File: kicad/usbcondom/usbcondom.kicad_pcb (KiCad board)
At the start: 4 copper layers, 44 x 29 mm, 21 parts, among them J1 Conn_02x10_Odd_Even, J2 Conn_02x10_Odd_Even, J3 USB-ID, J4 USB, U1 USBLC6-2

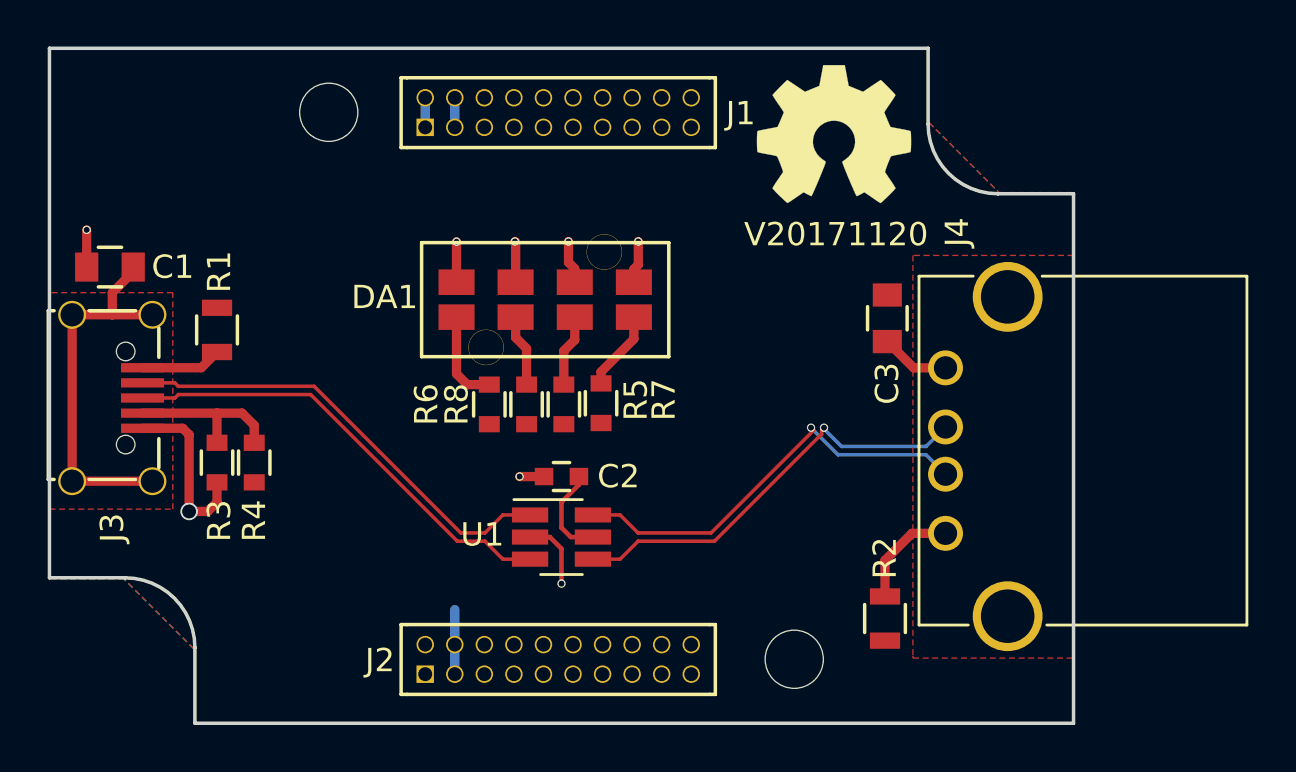
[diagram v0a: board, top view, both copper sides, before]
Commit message: updated silk, added proto area, replaced usb connectors
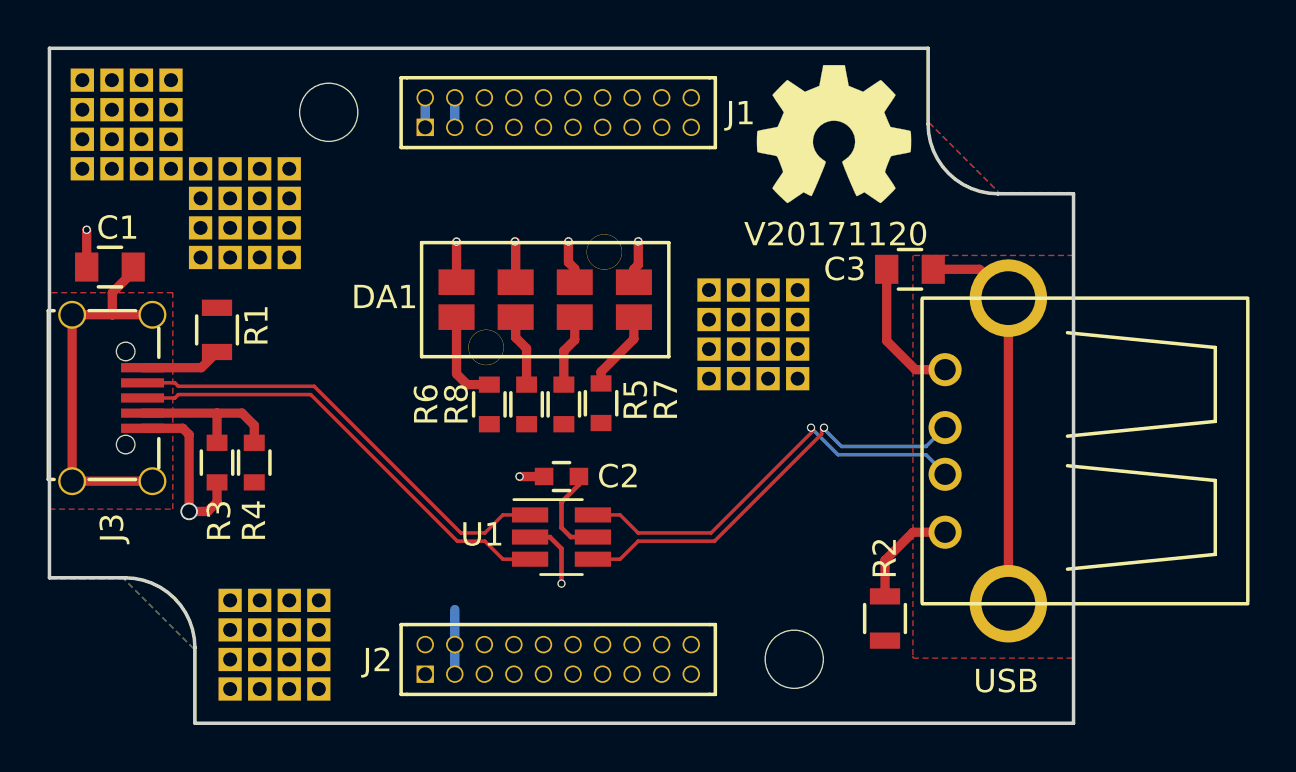
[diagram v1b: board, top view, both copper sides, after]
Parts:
- added J5: Proto, SquantorProto:proto-SMD-0127-04X04-P010-H006, F.Cu at (137.7, 111.1)
- added J6: Proto, SquantorProto:proto-SMD-0127-04X04-P010-H006, F.Cu at (158.2, 97.8)
- added J7: Proto, SquantorProto:proto-SMD-0127-04X04-P010-H006, F.Cu at (136.4, 92.6)
- added J8: Proto, SquantorProto:proto-SMD-0127-04X04-P010-H006, F.Cu at (131.3, 88.8)
- J4: footprint Connectors:USB_A -> SquantorUsb:USB-A-TH
- moved J4 4.45 mm to (169.2, 102.8), turned to 180 degrees
- moved C3 2.32 mm to (165.0, 95.0), turned to 0 degrees
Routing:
- net Net-(C3-Pad2): track 0.00 -> 16.9 mm
- net VSS: track 26.3 -> 29.4 mm

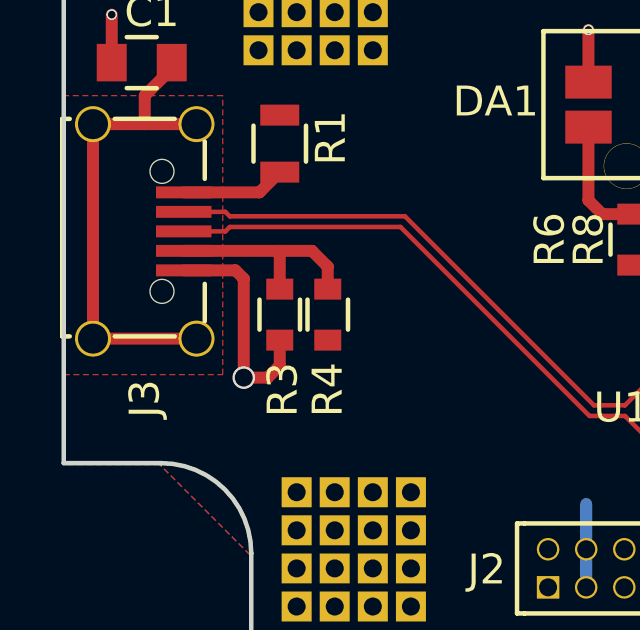
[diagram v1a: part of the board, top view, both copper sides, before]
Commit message: minor layout and silk screen updates
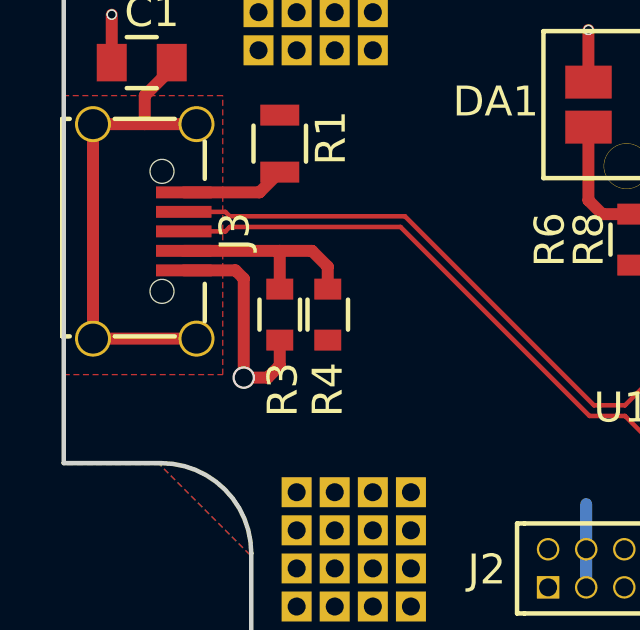
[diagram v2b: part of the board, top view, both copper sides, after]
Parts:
- J3: footprint SquantorUsb:SquantorUsb-USB-UB-SMD4H -> SquantorUsb:USB-muB-SMD_TH
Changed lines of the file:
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@@
   (general
     (links 42)
-    (no_connects 5)
+    (no_connects 0)
     (area 127.924999 85.424999 172.075001 114.575001)
     (thickness 1.6)
@@
       (net 36 /DIGITAL_15))
   )
-  (module SquantorUsb:SquantorUsb-USB-UB-SMD4H (layer F.Cu)
-    (at 130.7 100.525 270)
-    (fp_text reference J3 (at 5.575 0 270) (layer F.SilkS)
-      (effects (font (size 1 1) (thickness 0.15)))
-    )
-    (fp_text value USB-ID (at -0.381 -6.731 270) (layer F.Fab) hide
-      (effects (font (size 1 1) (thickness 0.15)))
-    )
-    (fp_line (start 3.5 2.5) (end 3.5 2.75) (layer F.SilkS) (width 0.15))
-    (fp_line (start 3.5 2.75) (end -3.75 2.75) (layer F.SilkS) (width 0.15))
-    (fp_line (start -3.75 2.75) (end -3.75 2.5) (layer F.SilkS) (width 0.15))
-    (fp_line (start -3.75 -1) (end -3.75 1) (layer F.SilkS) (width 0.15))
-    (fp_line (start 3.5 -1) (end 3.5 1) (layer F.SilkS) (width 0.15))
-    (fp_line (start 1.75 -2) (end 3 -2) (layer F.SilkS) (width 0.15))
-    (fp_line (start -3 -2) (end -1.75 -2) (layer F.SilkS) (width 0.15))
-    (pad S thru_hole circle (at -3.575 -1.725 270) (size 1.2 1.2) (drill 1) (layers *.Cu *.Mask)
-      (net 44 "Net-(C1-Pad2)"))
-    (pad S thru_hole circle (at 3.575 -1.725 270) (size 1.2 1.2) (drill 1) (layers *.Cu *.Mask)
-      (net 44 "Net-(C1-Pad2)"))
-    (pad S thru_hole circle (at -3.575 1.725 270) (size 1.2 1.2) (drill 1) (layers *.Cu *.Mask)
-      (net 44 "Net-(C1-Pad2)"))
-    (pad "" np_thru_hole circle (at -2 -0.575 270) (size 0.8 0.8) (drill 0.8) (layers *.Cu))
-    (pad 5 smd rect (at 1.3 -1.3 270) (size 0.4 1.85) (layers F.Cu F.Paste F.Mask)
-      (net 4 VSS))
-    (pad 4 smd rect (at 0.65 -1.3 270) (size 0.4 1.85) (layers F.Cu F.Paste F.Mask)
-      (net 37 "Net-(J3-Pad4)"))
-    (pad 3 smd rect (at 0 -1.3 270) (size 0.4 1.85) (layers F.Cu F.Paste F.Mask)
-      (net 38 /USB_IN_D+))
-    (pad 2 smd rect (at -0.65 -1.3 270) (size 0.4 1.85) (layers F.Cu F.Paste F.Mask)
-      (net 39 /USB_IN_D-))
-    (pad 1 smd rect (at -1.3 -1.3 270) (size 0.4 1.85) (layers F.Cu F.Paste F.Mask)
-      (net 40 "Net-(J3-Pad1)"))
-    (pad "" np_thru_hole circle (at 2 -0.575 270) (size 0.8 0.8) (drill 0.8) (layers *.Cu))
-    (pad S thru_hole circle (at 3.575 1.725 270) (size 1.2 1.2) (drill 1) (layers *.Cu *.Mask)
-      (net 44 "Net-(C1-Pad2)"))
-  )
   (module SquantorRcl:R_0805 (layer F.Cu)
     (at 163.9 110 270)
@@
       (net 43 "Net-(J4-Pad1)"))
   )
+  (module SquantorUsb:USB-muB-SMD_TH (layer F.Cu)
+    (at 130.7 100.525 270)
+    (fp_text reference J3 (at 0 -3 270) (layer F.SilkS)
+      (effects (font (size 1 1) (thickness 0.15)))
+    )
+    (fp_text value USB-ID (at 0 3.6 270) (layer F.Fab)
+      (effects (font (size 1 1) (thickness 0.15)))
+    )
+    (fp_line (start 3.5 2.5) (end 3.5 2.75) (layer F.SilkS) (width 0.15))
+    (fp_line (start 3.5 2.75) (end -3.75 2.75) (layer F.SilkS) (width 0.15))
+    (fp_line (start -3.75 2.75) (end -3.75 2.5) (layer F.SilkS) (width 0.15))
+    (fp_line (start -3.75 -1) (end -3.75 1) (layer F.SilkS) (width 0.15))
+    (fp_line (start 3.5 -1) (end 3.5 1) (layer F.SilkS) (width 0.15))
+    (fp_line (start 1.75 -2) (end 3 -2) (layer F.SilkS) (width 0.15))
+    (fp_line (start -3 -2) (end -1.75 -2) (layer F.SilkS) (width 0.15))
+    (pad S thru_hole circle (at -3.575 -1.725 270) (size 1.2 1.2) (drill 1) (layers *.Cu *.Mask)
+      (net 44 "Net-(C1-Pad2)"))
+    (pad S thru_hole circle (at 3.575 -1.725 270) (size 1.2 1.2) (drill 1) (layers *.Cu *.Mask)
+      (net 44 "Net-(C1-Pad2)"))
+    (pad S thru_hole circle (at -3.575 1.725 270) (size 1.2 1.2) (drill 1) (layers *.Cu *.Mask)
+      (net 44 "Net-(C1-Pad2)"))
+    (pad "" np_thru_hole circle (at -2 -0.575 270) (size 0.8 0.8) (drill 0.8) (layers *.Cu))
+    (pad 5 smd rect (at 1.3 -1.3 270) (size 0.4 1.85) (layers F.Cu F.Paste F.Mask)
+      (net 4 VSS))
+    (pad 4 smd rect (at 0.65 -1.3 270) (size 0.4 1.85) (layers F.Cu F.Paste F.Mask)
+      (net 37 "Net-(J3-Pad4)"))
+    (pad 3 smd rect (at 0 -1.3 270) (size 0.4 1.85) (layers F.Cu F.Paste F.Mask)
+      (net 38 /USB_IN_D+))
+    (pad 2 smd rect (at -0.65 -1.3 270) (size 0.4 1.85) (layers F.Cu F.Paste F.Mask)
+      (net 39 /USB_IN_D-))
+    (pad 1 smd rect (at -1.3 -1.3 270) (size 0.4 1.85) (layers F.Cu F.Paste F.Mask)
+      (net 40 "Net-(J3-Pad1)"))
+    (pad "" np_thru_hole circle (at 2 -0.575 270) (size 0.8 0.8) (drill 0.8) (layers *.Cu))
+    (pad S thru_hole circle (at 3.575 1.725 270) (size 1.2 1.2) (drill 1) (layers *.Cu *.Mask)
+      (net 44 "Net-(C1-Pad2)"))
+  )
   (gr_line (start 165.75 88.75) (end 165.75 85.5) (layer Edge.Cuts) (width 0.15))

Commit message: Changed to a 4 layer board
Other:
- copper layers 4 -> 2
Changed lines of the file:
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@@
     (links 42)
     (no_connects 0)
-    (area 127.924999 85.424999 172.075001 114.575001)
+    (area 126.198 84.348 179.689001 115.752)
     (thickness 1.6)
     (drawings 10)
@@
   (layers
     (0 F.Cu signal)
-    (1 In1.Cu signal)
-    (2 In2.Cu signal)
     (31 B.Cu signal)
     (32 B.Adhes user)
@@
   )
   (setup
-    (last_trace_width 0.4)
+    (last_trace_width 0.127)
     (user_trace_width 0.127)
     (user_trace_width 0.2)

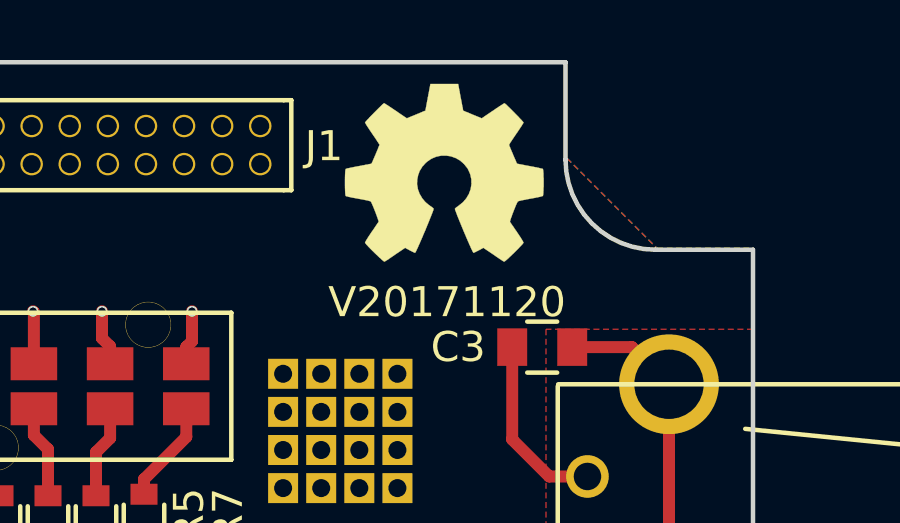
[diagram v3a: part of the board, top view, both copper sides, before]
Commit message: updated front fabrication, updated version number
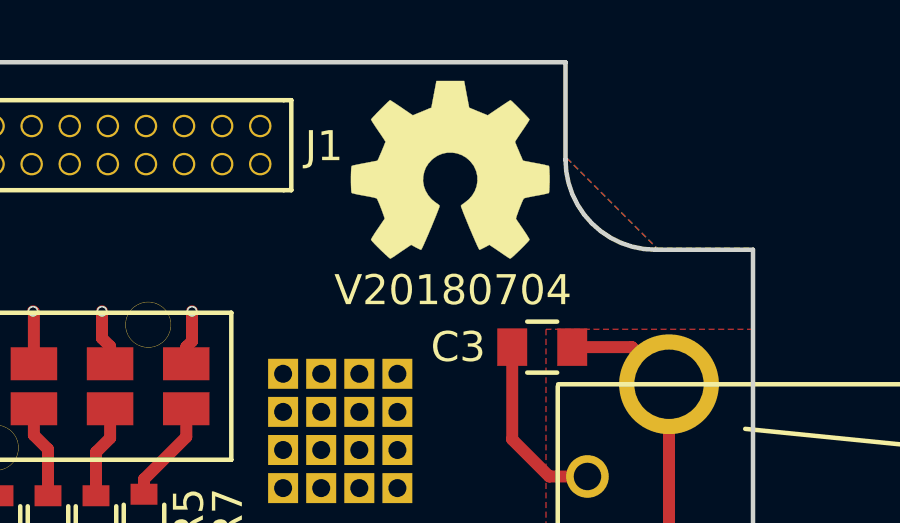
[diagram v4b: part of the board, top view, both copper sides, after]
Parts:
- N2: value V20171120 -> V20180704
- moved N2 15.1 mm to (162.0, 93.0)
- moved N1 0.22 mm to (161.9, 89.1)
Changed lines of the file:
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@@
     (links 42)
     (no_connects 0)
-    (area 126.198 84.348 179.689001 115.752)
+    (area 127.924999 85.424999 172.075001 114.575001)
     (thickness 1.6)
     (drawings 10)
@@
   )
   (module Symbols:OSHW-Symbol_6.7x6mm_SilkScreen (layer F.Cu)
-    (at 161.7 89.2)
+    (at 161.9 89.1)
     (descr "Open Source Hardware Symbol")
     (tags "Logo Symbol OSHW")
@@
   )
   (module SquantorLabels:Label_version (layer F.Cu)
-    (at 150.4 102.7)
+    (at 162 93)
     (fp_text reference N2 (at 0 2) (layer F.Fab) hide
       (effects (font (size 1 1) (thickness 0.15)))
     )
-    (fp_text value V20171120 (at 11.4 -9.2) (layer F.SilkS)
+    (fp_text value V20180704 (at 0 0.1) (layer F.SilkS)
       (effects (font (size 1 1) (thickness 0.15)))
     )
@@
       (effects (font (size 1 1) (thickness 0.15)))
     )
-    (fp_text value FB (at 0 2.1 270) (layer F.Fab)
+    (fp_text value FB (at -0.1 0 270) (layer F.Fab)
       (effects (font (size 1 1) (thickness 0.15)))
     )
@@
       (effects (font (size 1 1) (thickness 0.15)))
     )
-    (fp_text value C (at 0 2.1) (layer F.Fab)
+    (fp_text value C (at 0 0.1) (layer F.Fab)
       (effects (font (size 1 1) (thickness 0.15)))
     )
@@
       (effects (font (size 1 1) (thickness 0.15)))
     )
-    (fp_text value C (at 0 2.1) (layer F.Fab)
+    (fp_text value C (at 0.027 0.004) (layer F.Fab)
       (effects (font (size 1 1) (thickness 0.15)))
     )
@@
       (effects (font (size 1 1) (thickness 0.15)))
     )
-    (fp_text value FB (at 0 2.1 270) (layer F.Fab)
+    (fp_text value FB (at 0 -0.1 270) (layer F.Fab)
       (effects (font (size 1 1) (thickness 0.15)))
     )
@@
       (effects (font (size 1 1) (thickness 0.15)))
     )
-    (fp_text value R (at 0 1.9 270) (layer F.Fab)
+    (fp_text value R (at 0 0 270) (layer F.Fab)
       (effects (font (size 1 1) (thickness 0.15)))
     )
@@
       (effects (font (size 1 1) (thickness 0.15)))
     )
-    (fp_text value R (at 0.85 -4.7 270) (layer F.Fab)
-      (effects (font (size 1 1) (thickness 0.15)))
-    )
+    (fp_text value R (at 0 -0.1 270) (layer F.Fab)
+      (effects (font (size 1 1) (thickness 0.15)))
+    )

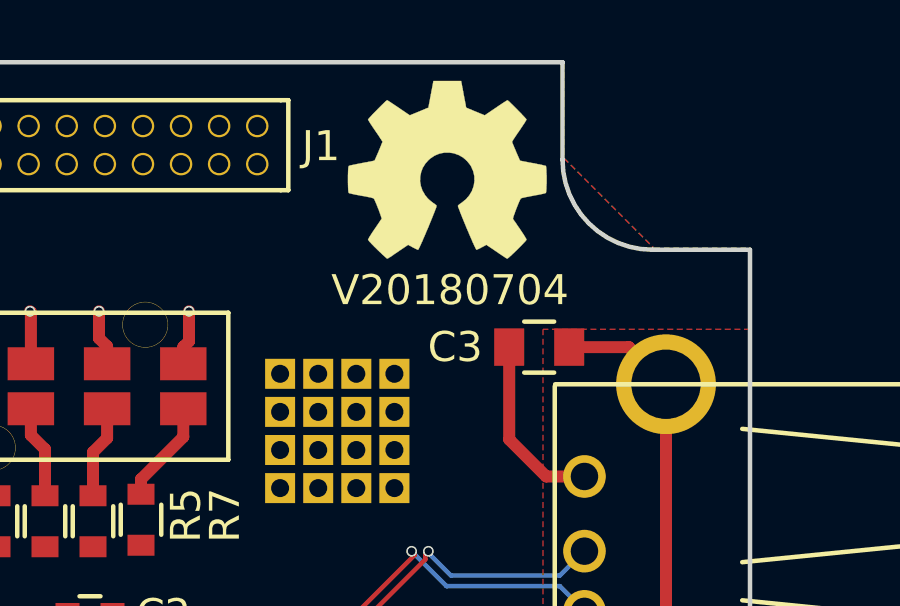
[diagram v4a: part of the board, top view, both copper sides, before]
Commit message: updates to usb condom
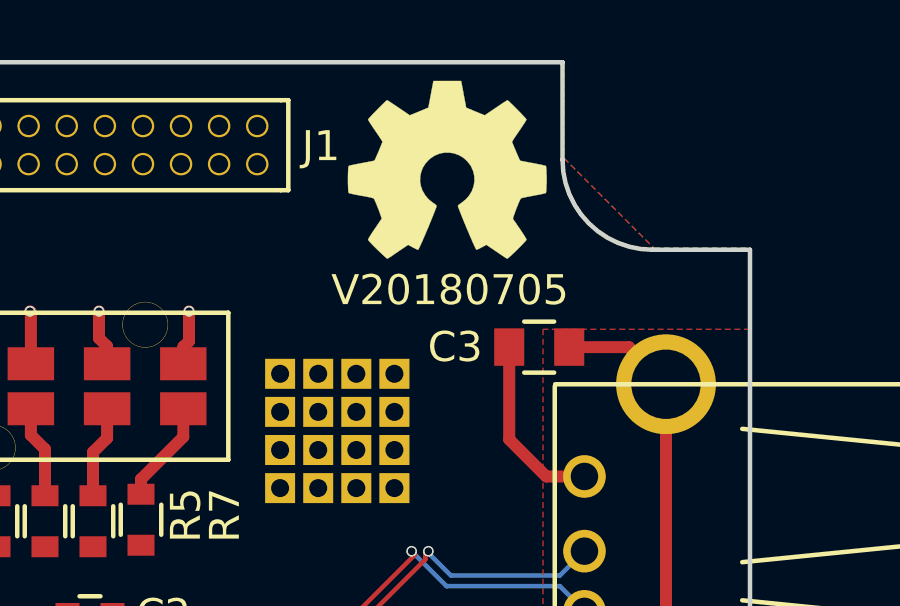
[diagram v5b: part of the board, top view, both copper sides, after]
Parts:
- N2: value V20180704 -> V20180705
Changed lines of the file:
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@@
       (effects (font (size 1 1) (thickness 0.15)))
     )
-    (fp_text value V20180704 (at 0 0.1) (layer F.SilkS)
+    (fp_text value V20180705 (at 0 0.1) (layer F.SilkS)
       (effects (font (size 1 1) (thickness 0.15)))
     )
